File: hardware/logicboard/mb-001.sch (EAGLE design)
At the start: 31 parts, among them IC1 74ALS05N, IC2 LTC485N, IC3 LTC485N, J0 DC5V, J1 DIN5, J2 DIN5, J3 DIN5, X1 NELTRON-7810-XPXC, X2 NELTRON-7810-XPXC

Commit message: Initial design.
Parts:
- removed C1: 100n, rcl:C-EU025-024X044
- removed C2, C3, C4, C5: 10n, rcl:C-EU025-024X044
- removed D1: DIODE-1N4148, SparkFun-DiscreteSemi:DIODE-1N4148
- removed IC1: 74ALS05N, 74xx-us:74ALS05N
- removed IC2, IC3: LTC485N, linear-technology:LTC485N
- removed J0: DC5V, con-jack:JACK-PLUG0
- removed LED1: BLUE, led:LED3MM
- removed LED2, LED3: YELLOW, led:LED3MM
- removed OK1: HCPL2630, optocoupler:HCPL2630
- removed R1, R2, R3, R4, R5: 220, rcl:R-EU_0204/5
- removed R6L1, R7L2, R8L3: 1k, rcl:R-EU_0204/5
- removed R9: 100, rcl:R-EU_0204/5
- removed RN2: 4.7k, resistor-net:RN04
- removed X1, X2: NELTRON-7810-XPXC, con-rj45:NELTRON-7810-XPXC
- added J4, J5, J6: AUDIO_JACK_3.5MM_KIT, SparkFun-Connectors:AUDIO_JACK_3.5MM_KIT
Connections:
- removed net GND: C1.2, C2.2, C3.2, C4.2, C5.2, IC2.!RE, IC2.DE, IC2.DI, IC2.GND, IC3.GND, J0.1, J0.2, J2.2, J3.2, LED1.C, OK1A.GND, OK1B.A2, OK1B.C2, X1.S1, X1.S2, X2.S1, X2.S2
- removed net MIDIIN: D1.C, OK1A.A1, R1.2
- removed net MIDIOUT: IC1E.O, R3.2
- removed net MIDITHRU: IC1B.O, R5.2
- removed net MIRTN: D1.A, J1.5, OK1A.C1
- removed net MISND: J1.4, R1.1
- removed net MORTN: J2.5, R3.1
- removed net MOSND: J2.4, R2.1
- removed net MTRTN: J3.5, R5.1
- removed net MTSND: J3.4, R4.1
- removed net N$1: IC1C.O, LED2.C
- removed net N$2: LED3.A, R8L3.1
- removed net N$3: IC1F.O, LED3.C
- removed net N$4: LED1.A, R6L1.1
- removed net N$5: LED2.A, R7L2.1
- removed net NMIDIOUT: IC1D.O, IC1E.I, RN2.5
- removed net NMIDITHRU: IC1A.O, IC1B.I, RN2.3
- removed net RX: IC1D.I, IC1F.I, IC2.RO
- removed net RX+: IC2.A, R9.1, X2.1
- removed net RX-: IC2.B, R9.2, X2.2
- removed net TX: IC1A.I, IC1C.I, IC3.DI, OK1A.VO1, RN2.2
- removed net TX+: IC3.A, X1.1
- removed net TX-: IC3.B, X1.2
- removed net VCC: C1.1, C2.1, C3.1, C4.1, C5.1, IC2.VCC, IC3.!RE, IC3.DE, IC3.VCC, J0.3, OK1A.VCC, R2.2, R4.2, R6L1.2, R7L2.2, R8L3.2, RN2.1
- new net M1GND: J1.2, J4.SLEEVE
- new net M1RTN: J1.5, J4.TIP
- new net M1SND: J1.4, J4.RING
- new net M2GND: J2.2, J5.SLEEVE
- new net M2RTN: J2.5, J5.TIP
- new net M2SND: J2.4, J5.RING
- new net M3GND: J3.2, J6.SLEEVE
- new net M3RTN: J3.5, J6.TIP
- new net M3SND: J3.4, J6.RING
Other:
- note added: "MIDI 1"
- note added: "MIDI 2"
- note added: "MIDI 3"
- note removed: "MIDI IN"
- note removed: "MIDI OUT"
- note removed: "MIDI THRU"
- moved on the sheet: J2, J3

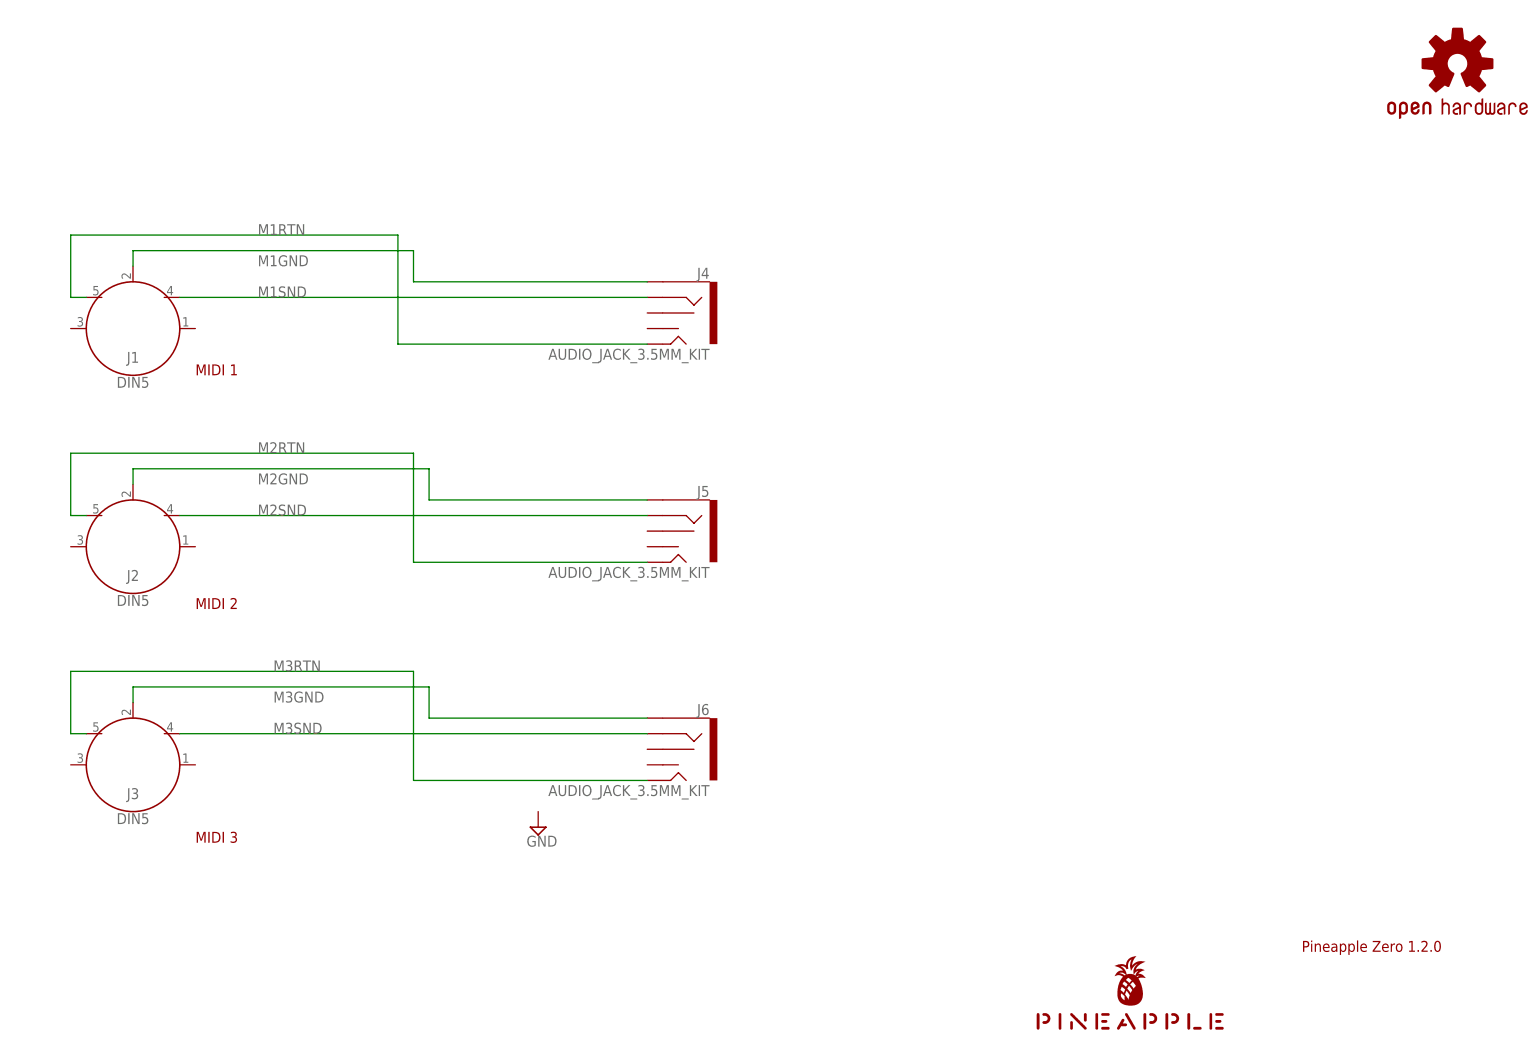
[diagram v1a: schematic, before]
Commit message: Type A/B Sw.
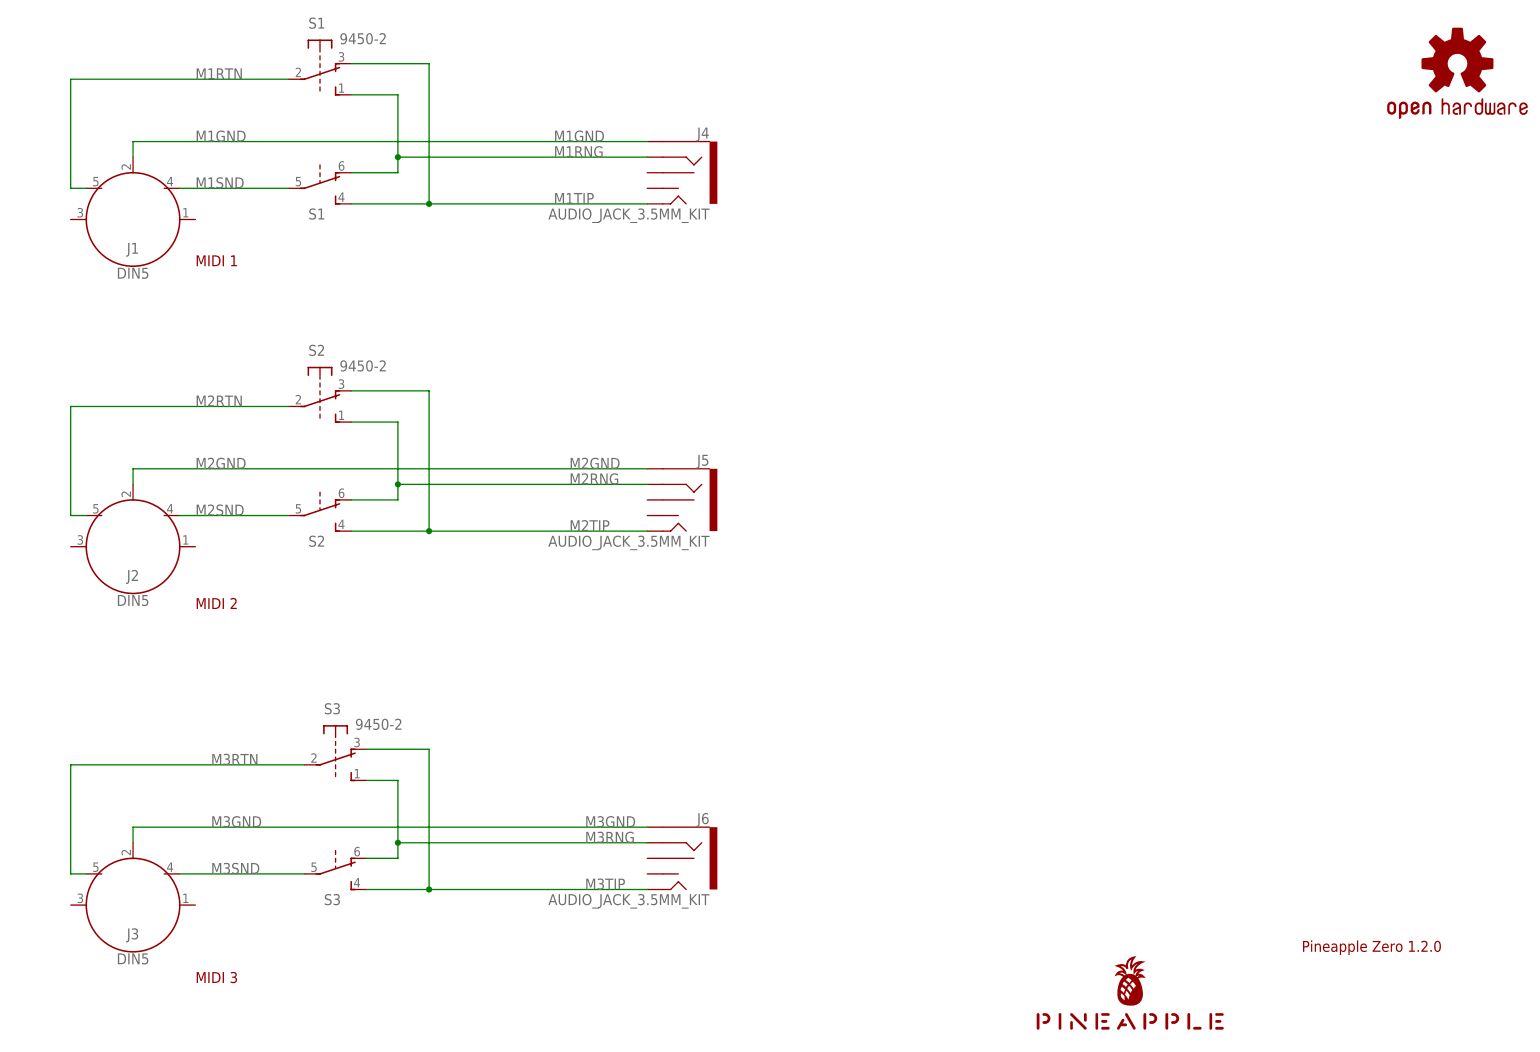
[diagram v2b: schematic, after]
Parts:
- added S1, S2, S3: 9450-2, switch-misc:9450-2
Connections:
- new net M1RNG: J4.RING, S11.S, S12.O
- new net M1TIP: J4.TIP, S11.O, S12.S
- new net M2RNG: J5.RING, S21.S, S22.O
- new net M2TIP: J5.TIP, S21.O, S22.S
- new net M3RNG: J6.RING, S31.S, S32.O
- new net M3TIP: J6.TIP, S31.O, S32.S
- net M1RTN: now also S11.P; no longer J4.TIP
- net M1SND: now also S12.P; no longer J4.RING
- net M2RTN: now also S21.P; no longer J5.TIP
- net M2SND: now also S22.P; no longer J5.RING
- net M3RTN: now also S31.P; no longer J6.TIP
- net M3SND: now also S32.P; no longer J6.RING
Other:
- moved on the sheet: J1, J3, J4, J5, J6

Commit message: Symbol name.
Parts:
- renumbered J4 to JJ1, J5 to JJ2, J6 to JJ3
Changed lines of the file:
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@@
 <part name="J2" library="SparkFun-Connectors" library_urn="urn:adsk.eagle:library:513" deviceset="DIN5" device="" package3d_urn="urn:adsk.eagle:package:38294/1"/>
 <part name="J3" library="SparkFun-Connectors" library_urn="urn:adsk.eagle:library:513" deviceset="DIN5" device="" package3d_urn="urn:adsk.eagle:package:38294/1"/>
-<part name="J4" library="SparkFun-Connectors" library_urn="urn:adsk.eagle:library:513" deviceset="AUDIO_JACK_3.5MM" device="_KIT" package3d_urn="urn:adsk.eagle:package:38014/1"/>
-<part name="J5" library="SparkFun-Connectors" library_urn="urn:adsk.eagle:library:513" deviceset="AUDIO_JACK_3.5MM" device="_KIT" package3d_urn="urn:adsk.eagle:package:38014/1"/>
-<part name="J6" library="SparkFun-Connectors" library_urn="urn:adsk.eagle:library:513" deviceset="AUDIO_JACK_3.5MM" device="_KIT" package3d_urn="urn:adsk.eagle:package:38014/1"/>
+<part name="JJ1" library="SparkFun-Connectors" library_urn="urn:adsk.eagle:library:513" deviceset="AUDIO_JACK_3.5MM" device="_KIT" package3d_urn="urn:adsk.eagle:package:38014/1"/>
+<part name="JJ2" library="SparkFun-Connectors" library_urn="urn:adsk.eagle:library:513" deviceset="AUDIO_JACK_3.5MM" device="_KIT" package3d_urn="urn:adsk.eagle:package:38014/1"/>
+<part name="JJ3" library="SparkFun-Connectors" library_urn="urn:adsk.eagle:library:513" deviceset="AUDIO_JACK_3.5MM" device="_KIT" package3d_urn="urn:adsk.eagle:package:38014/1"/>
 <part name="S1" library="switch-misc" library_urn="urn:adsk.eagle:library:376" deviceset="9450-2" device="" package3d_urn="urn:adsk.eagle:package:27434/1"/>
 <part name="S2" library="switch-misc" library_urn="urn:adsk.eagle:library:376" deviceset="9450-2" device="" package3d_urn="urn:adsk.eagle:package:27434/1"/>
@@
 <attribute name="VALUE" x="25.4" y="20.066" size="1.778" layer="96" font="vector" align="top-center"/>
 </instance>
-<instance part="J4" gate="G$1" x="114.3" y="147.32" smashed="yes" rot="MR0">
+<instance part="JJ1" gate="G$1" x="114.3" y="147.32" smashed="yes" rot="MR0">
 <attribute name="NAME" x="119.38" y="152.908" size="1.778" layer="95" font="vector" rot="MR0"/>
 <attribute name="VALUE" x="119.38" y="139.7" size="1.778" layer="96" font="vector" rot="MR0"/>
 </instance>
-<instance part="J5" gate="G$1" x="114.3" y="93.98" smashed="yes" rot="MR0">
+<instance part="JJ2" gate="G$1" x="114.3" y="93.98" smashed="yes" rot="MR0">
 <attribute name="NAME" x="119.38" y="99.568" size="1.778" layer="95" font="vector" rot="MR0"/>
 <attribute name="VALUE" x="119.38" y="86.36" size="1.778" layer="96" font="vector" rot="MR0"/>
 </instance>
-<instance part="J6" gate="G$1" x="114.3" y="35.56" smashed="yes" rot="MR0">
+<instance part="JJ3" gate="G$1" x="114.3" y="35.56" smashed="yes" rot="MR0">
 <attribute name="NAME" x="119.38" y="41.148" size="1.778" layer="95" font="vector" rot="MR0"/>
 <attribute name="VALUE" x="119.38" y="27.94" size="1.778" layer="96" font="vector" rot="MR0"/>
@@
 <wire x1="25.4" y1="149.86" x2="25.4" y2="152.4" width="0.1524" layer="91"/>
 <wire x1="25.4" y1="152.4" x2="109.22" y2="152.4" width="0.1524" layer="91"/>
-<pinref part="J4" gate="G$1" pin="SLEEVE"/>
+<pinref part="JJ1" gate="G$1" pin="SLEEVE"/>
 <label x="35.56" y="152.4" size="1.778" layer="95"/>
 <label x="93.98" y="152.4" size="1.778" layer="95"/>
@@
 <wire x1="25.4" y1="38.1" x2="25.4" y2="40.64" width="0.1524" layer="91"/>
 <wire x1="25.4" y1="40.64" x2="109.22" y2="40.64" width="0.1524" layer="91"/>
-<pinref part="J6" gate="G$1" pin="SLEEVE"/>
+<pinref part="JJ3" gate="G$1" pin="SLEEVE"/>
 <label x="38.1" y="40.64" size="1.778" layer="95"/>
 <label x="99.06" y="40.64" size="1.778" layer="95"/>
@@
 <wire x1="25.4" y1="96.52" x2="25.4" y2="99.06" width="0.1524" layer="91"/>
 <wire x1="25.4" y1="99.06" x2="109.22" y2="99.06" width="0.1524" layer="91"/>
-<pinref part="J5" gate="G$1" pin="SLEEVE"/>
+<pinref part="JJ2" gate="G$1" pin="SLEEVE"/>
 <label x="35.56" y="99.06" size="1.778" layer="95"/>
 <label x="96.52" y="99.06" size="1.778" layer="95"/>
@@
 <pinref part="S1" gate="1" pin="O"/>
 <wire x1="60.96" y1="165.1" x2="73.66" y2="165.1" width="0.1524" layer="91"/>
-<pinref part="J4" gate="G$1" pin="TIP"/>
+<pinref part="JJ1" gate="G$1" pin="TIP"/>
 <wire x1="73.66" y1="165.1" x2="73.66" y2="142.24" width="0.1524" layer="91"/>
 <wire x1="73.66" y1="142.24" x2="109.22" y2="142.24" width="0.1524" layer="91"/>
@@
 <net name="M1RNG" class="0">
 <segment>
-<pinref part="J4" gate="G$1" pin="RING"/>
+<pinref part="JJ1" gate="G$1" pin="RING"/>
 <wire x1="109.22" y1="149.86" x2="68.58" y2="149.86" width="0.1524" layer="91"/>
 <wire x1="68.58" y1="149.86" x2="68.58" y2="147.32" width="0.1524" layer="91"/>
@@
 <wire x1="60.96" y1="111.76" x2="73.66" y2="111.76" width="0.1524" layer="91"/>
 <wire x1="73.66" y1="111.76" x2="73.66" y2="88.9" width="0.1524" layer="91"/>
-<pinref part="J5" gate="G$1" pin="TIP"/>
+<pinref part="JJ2" gate="G$1" pin="TIP"/>
 <wire x1="73.66" y1="88.9" x2="109.22" y2="88.9" width="0.1524" layer="91"/>
 <pinref part="S2" gate="2" pin="S"/>
@@
 <wire x1="60.96" y1="106.68" x2="68.58" y2="106.68" width="0.1524" layer="91"/>
 <wire x1="68.58" y1="106.68" x2="68.58" y2="96.52" width="0.1524" layer="91"/>
-<pinref part="J5" gate="G$1" pin="RING"/>
+<pinref part="JJ2" gate="G$1" pin="RING"/>
 <wire x1="68.58" y1="96.52" x2="109.22" y2="96.52" width="0.1524" layer="91"/>
 <wire x1="68.58" y1="96.52" x2="68.58" y2="93.98" width="0.1524" layer="91"/>
@@
 <wire x1="63.5" y1="53.34" x2="73.66" y2="53.34" width="0.1524" layer="91"/>
 <wire x1="73.66" y1="53.34" x2="73.66" y2="30.48" width="0.1524" layer="91"/>
-<pinref part="J6" gate="G$1" pin="TIP"/>
+<pinref part="JJ3" gate="G$1" pin="TIP"/>
 <wire x1="73.66" y1="30.48" x2="109.22" y2="30.48" width="0.1524" layer="91"/>
 <pinref part="S3" gate="2" pin="S"/>
@@
 <wire x1="68.58" y1="38.1" x2="68.58" y2="35.56" width="0.1524" layer="91"/>
 <wire x1="68.58" y1="35.56" x2="63.5" y2="35.56" width="0.1524" layer="91"/>
-<pinref part="J6" gate="G$1" pin="RING"/>
+<pinref part="JJ3" gate="G$1" pin="RING"/>
 <wire x1="109.22" y1="38.1" x2="68.58" y2="38.1" width="0.1524" layer="91"/>
 <junction x="68.58" y="38.1"/>

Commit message: Symbol name.
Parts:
- renumbered J1 to J7, J2 to J8, J3 to J9, JJ1 to JJ7, JJ2 to JJ8, JJ3 to JJ9

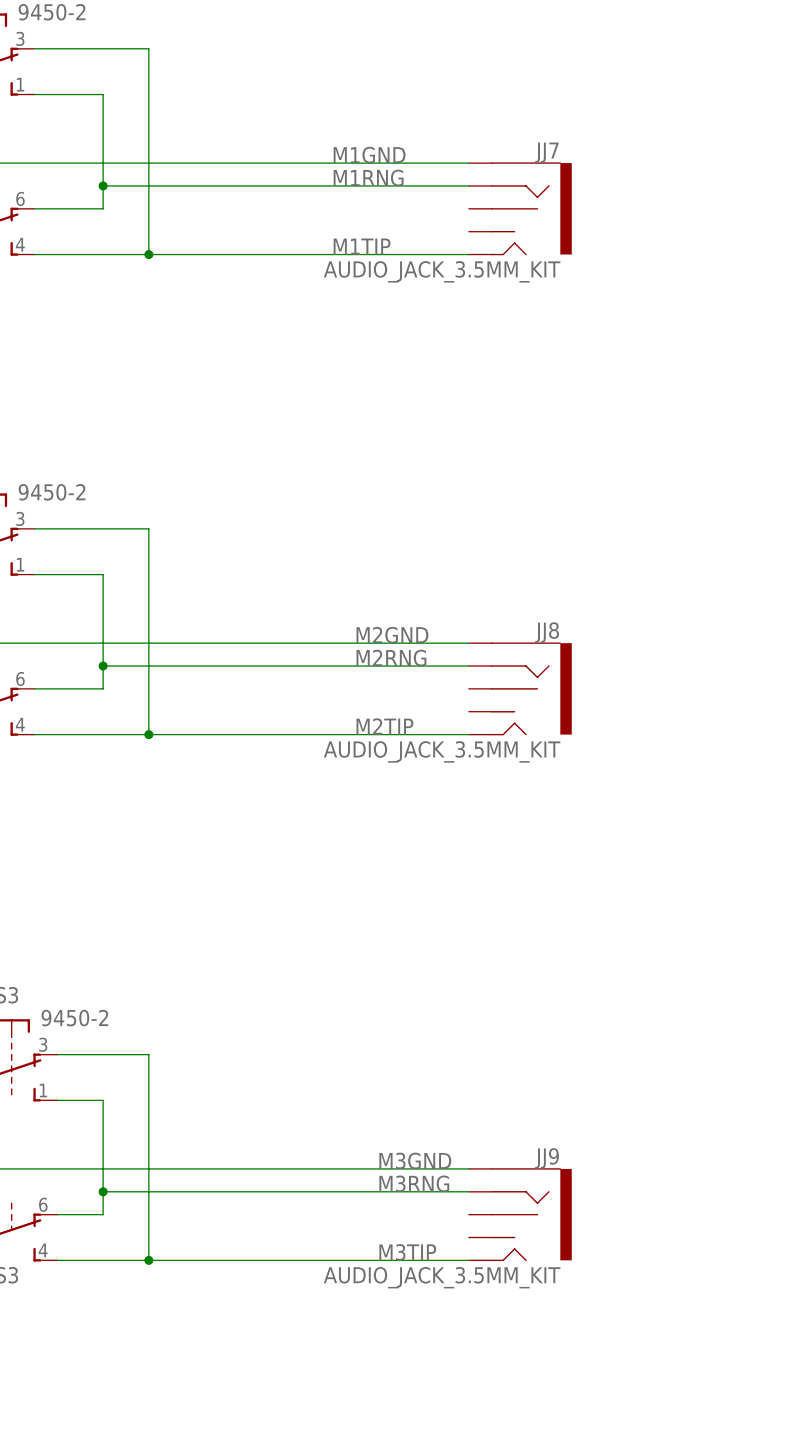
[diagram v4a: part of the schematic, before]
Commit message: Fixed silk and signal names. No pattern changed.
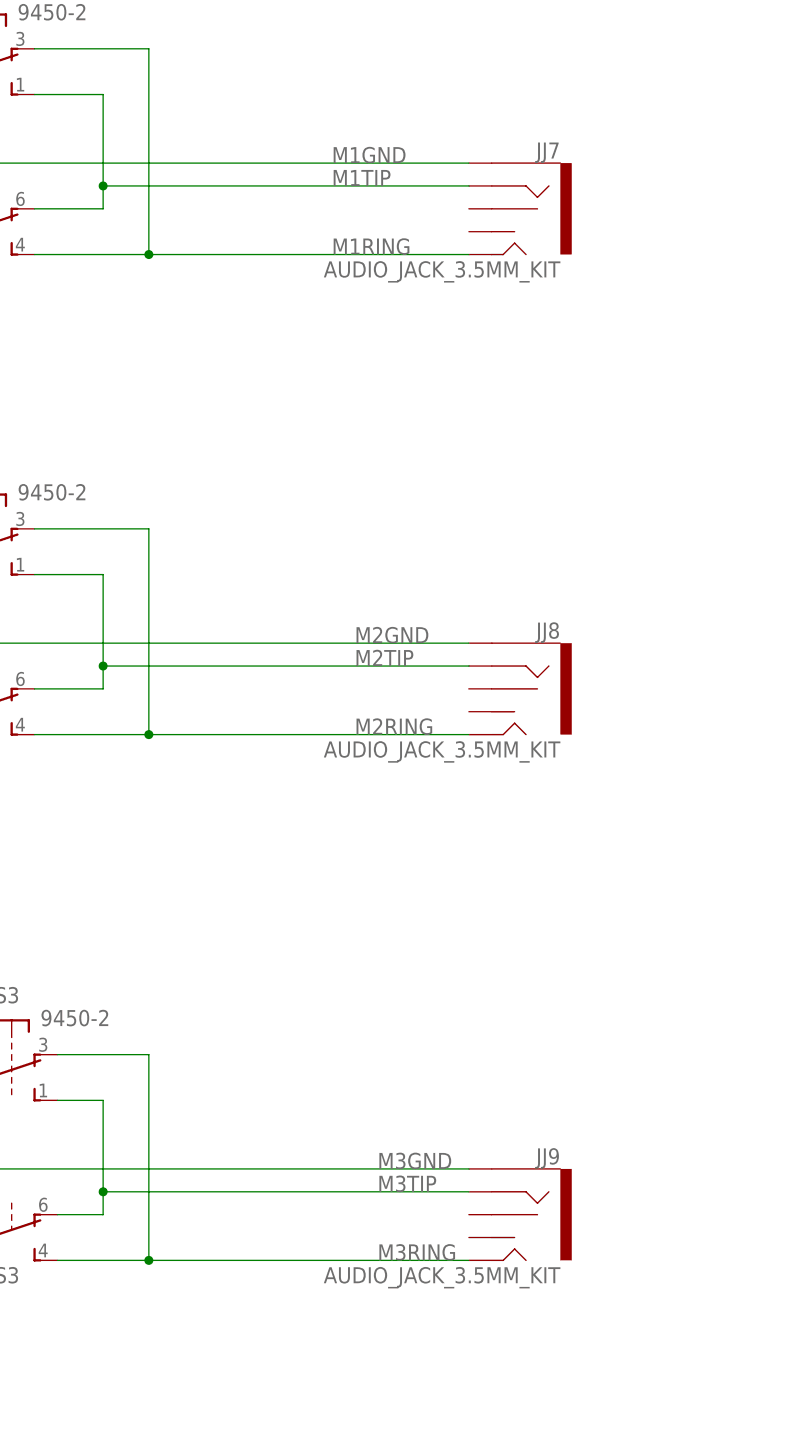
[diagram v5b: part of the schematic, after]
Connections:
- removed net M1RNG: JJ7.RING, S11.S, S12.O
- removed net M2RNG: JJ8.RING, S21.S, S22.O
- removed net M3RNG: JJ9.RING, S31.S, S32.O
- new net M1RING: JJ7.TIP, S11.O, S12.S
- new net M2RING: JJ8.TIP, S21.O, S22.S
- new net M3RING: JJ9.TIP, S31.O, S32.S
- net M1TIP: now also JJ7.RING, S11.S, S12.O; no longer JJ7.TIP, S11.O, S12.S
- net M2TIP: now also JJ8.RING, S21.S, S22.O; no longer JJ8.TIP, S21.O, S22.S
- net M3TIP: now also JJ9.RING, S31.S, S32.O; no longer JJ9.TIP, S31.O, S32.S
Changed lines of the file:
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@@
 </segment>
 </net>
-<net name="M1TIP" class="0">
+<net name="M1RING" class="0">
 <segment>
 <pinref part="S1" gate="1" pin="O"/>
@@
 </segment>
 </net>
-<net name="M1RNG" class="0">
+<net name="M1TIP" class="0">
 <segment>
 <pinref part="JJ7" gate="G$1" pin="RING"/>
@@
 </segment>
 </net>
-<net name="M2TIP" class="0">
+<net name="M2RING" class="0">
 <segment>
 <pinref part="S2" gate="1" pin="O"/>
@@
 </segment>
 </net>
-<net name="M2RNG" class="0">
+<net name="M2TIP" class="0">
 <segment>
 <pinref part="S2" gate="1" pin="S"/>
@@
 </segment>
 </net>
-<net name="M3TIP" class="0">
+<net name="M3RING" class="0">
 <segment>
 <pinref part="S3" gate="1" pin="O"/>
@@
 </segment>
 </net>
-<net name="M3RNG" class="0">
+<net name="M3TIP" class="0">
 <segment>
 <pinref part="S3" gate="1" pin="S"/>
